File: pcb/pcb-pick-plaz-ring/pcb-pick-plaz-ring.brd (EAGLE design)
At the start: 32 x 32 mm, 27 parts, among them X1 PIN_1X1SMD_BIG_L, X2 PIN_1X1SMD_BIG_L

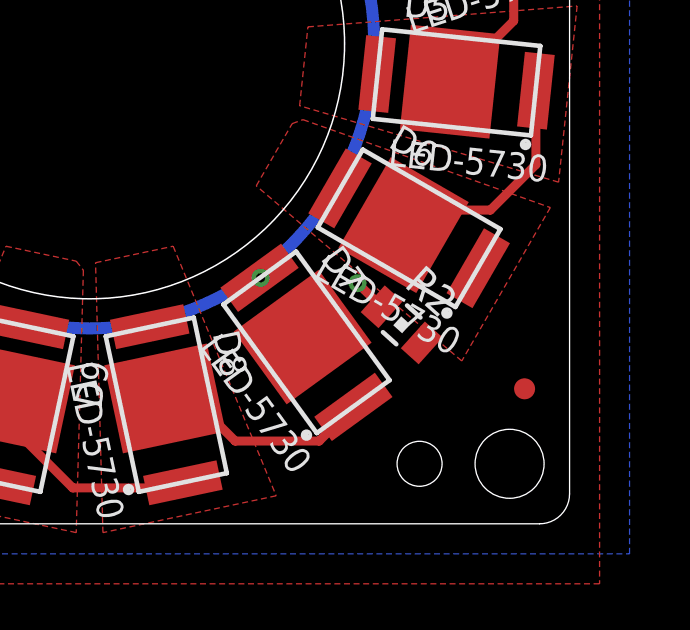
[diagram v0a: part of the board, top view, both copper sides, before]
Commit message: pcb missing trace fix
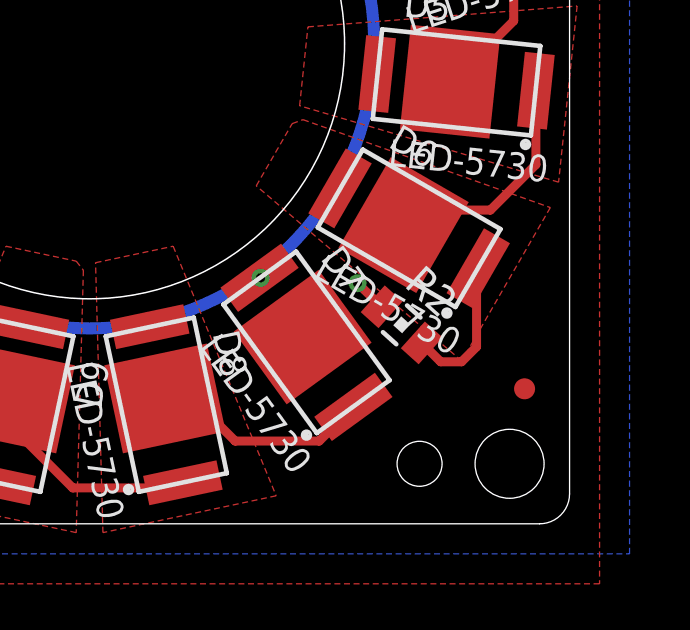
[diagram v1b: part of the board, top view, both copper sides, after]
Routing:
- net N$6: track 0.00 -> 4.94 mm
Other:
- board text added: "pcb-pick-plaz-ring v1b by ftobler 2021"
- board text removed: "pcb-pick-plaz-ring v1 by ftobler 2021"
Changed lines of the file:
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@@
 <wire x1="13.8" y1="7.1" x2="14.2" y2="6.2" width="0.1" layer="41"/>
 <wire x1="-12.2" y1="10.7" x2="-15.7" y2="10.7" width="0.1" layer="41"/>
-<text x="4" y="12.9" size="1" layer="34" rot="MR0">pcb-pick-plaz-ring v1
+<text x="4" y="12.9" size="1" layer="34" rot="MR0">pcb-pick-plaz-ring v1b
 by ftobler 2021</text>
 <rectangle x1="-16" y1="6.1" x2="-9" y2="7.9" layer="34"/>
@@
 <contactref element="D6" pad="C"/>
 <contactref element="R2" pad="2"/>
-<wire x1="11.07285625" y1="-9.97004375" x2="12.9557375" y2="-7.48" width="0" layer="19" extent="1-1"/>
+<wire x1="11.07285625" y1="-9.97004375" x2="11.7028125" y2="-10.6" width="0.3" layer="1"/>
+<wire x1="11.7028125" y1="-10.6" x2="12.4" y2="-10.6" width="0.3" layer="1"/>
+<wire x1="12.4" y1="-10.6" x2="12.9" y2="-10.1" width="0.3" layer="1"/>
+<wire x1="12.9" y1="-7.5357375" x2="12.9557375" y2="-7.48" width="0.3" layer="1"/>
+<wire x1="12.9" y1="-10.1" x2="12.9" y2="-7.5357375" width="0.3" layer="1"/>
 </signal>
 <signal name="N$7">
